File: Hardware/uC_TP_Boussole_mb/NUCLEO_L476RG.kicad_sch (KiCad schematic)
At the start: 40 parts, among them J501 Conn_01x06, J502 Conn_01x06, J503 Conn_01x06, SW501 SW_Push, SW502 SW_Push, SW503 SW_Push, SW504 SW_Push, SW505 SW_Push, U501 NUCLEO_L476RG

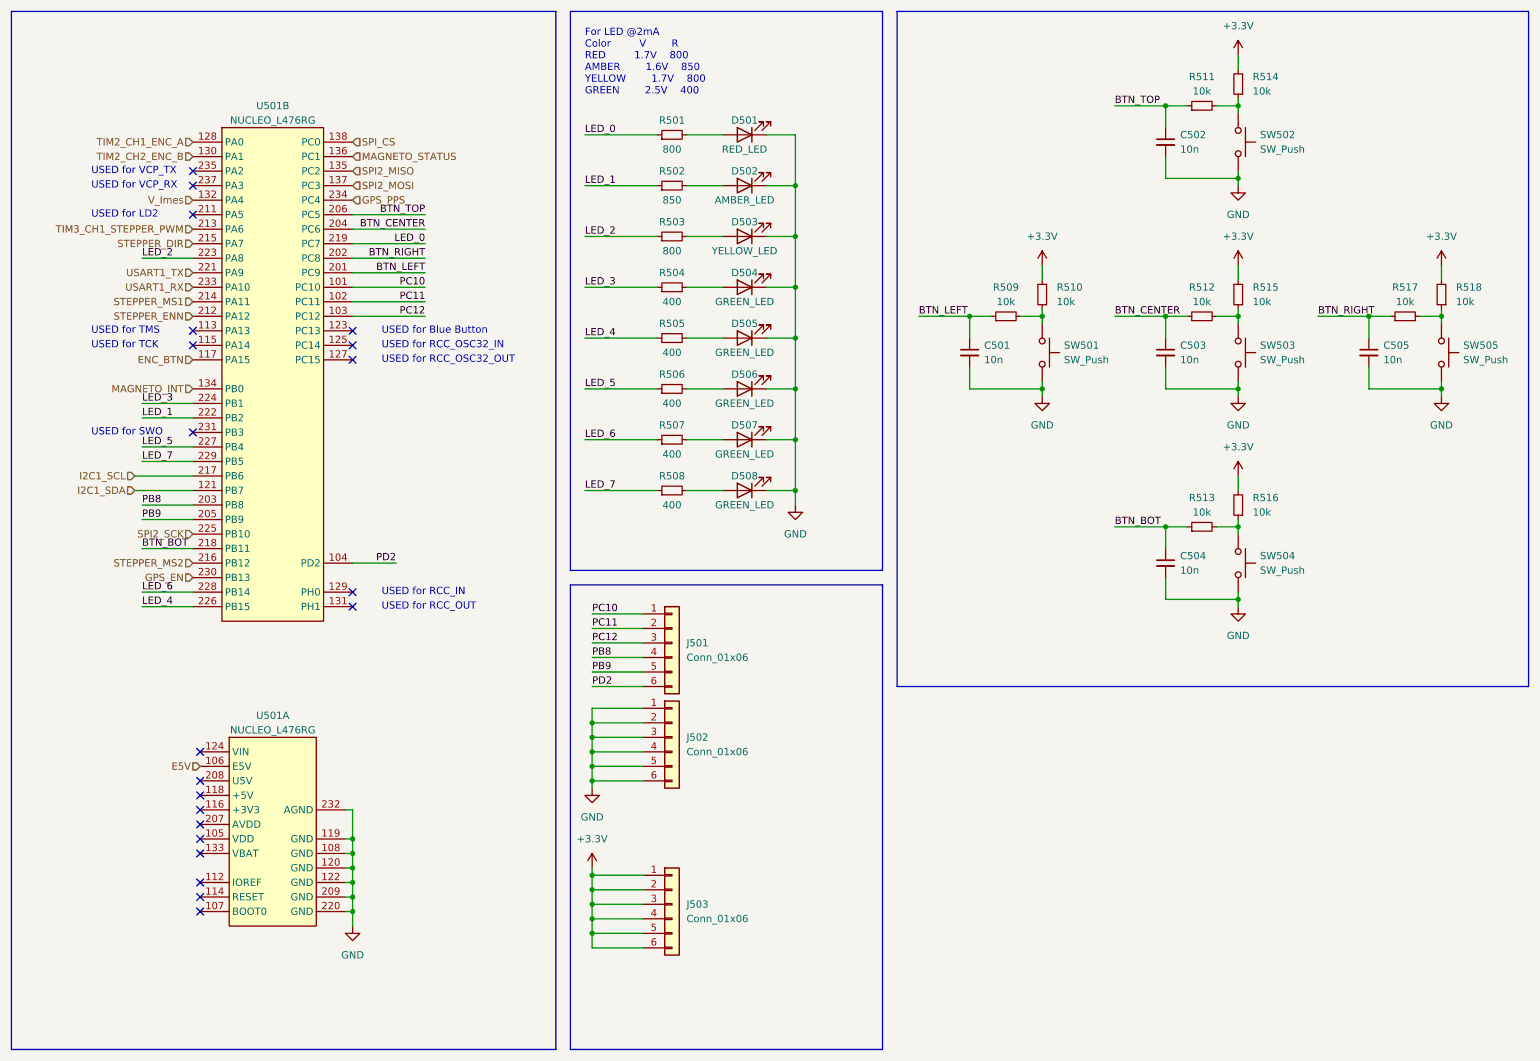
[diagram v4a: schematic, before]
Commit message: update schematic
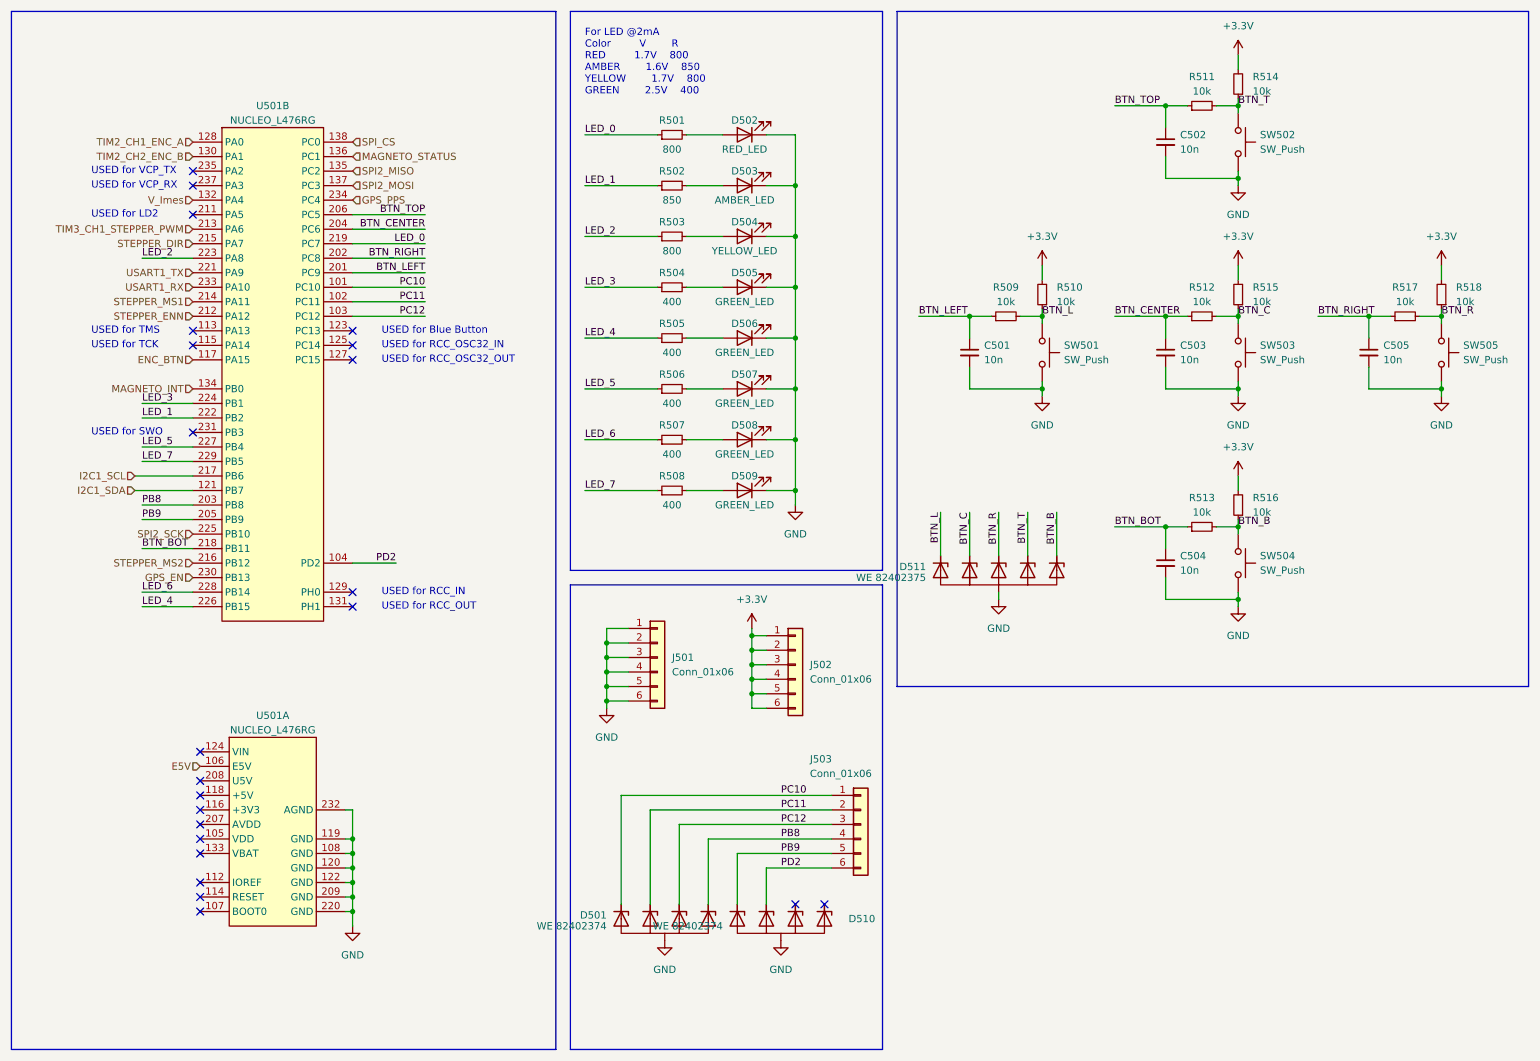
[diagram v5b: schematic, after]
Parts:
- added D501, D510: WE 82402374, libs:SC70-5L, symbol mylibs:D_TVS_Uni_x4
- added D511: WE 82402375, libs:SC70-6L, symbol mylibs:D_TVS_Uni_x5
- renumbered D501 to D502, D502 to D503, D503 to D504, D504 to D505, D505 to D506, D506 to D507, D507 to D508, D508 to D509, J502 to J501, J503 to J502, J501 to J503
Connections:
- net GND: now also D501.2 (GND), D510.2 (GND), D511.2 (GND)
- net PB8: now also D501.1 (I/O)
- net PB9: now also D510.5 (I/O)
- net PC10: now also D501.5 (I/O)
- net PC11: now also D501.4 (I/O)
- net PC12: now also D501.3 (I/O)
- net PD2: now also D510.4 (I/O)
- net BTN_R: now reaches R517.2, R518.1, SW505.1
- net BTN_R: now also D511.4 (I/O)
- net BTN_C: now reaches R512.2, R515.1, SW503.1
- net BTN_C: now also D511.5 (I/O)
- net BTN_L: now reaches R509.2, R510.1, SW501.1
- net BTN_L: now also D511.6 (I/O)
- net BTN_T: now reaches R511.2, R514.1, SW502.1
- net BTN_T: now also D511.3 (I/O)
- net BTN_B: now reaches R513.2, R516.1, SW504.1
- net BTN_B: now also D511.1 (I/O)
- no-connect marks 21 -> 23
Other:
- moved on the sheet: J501, J502, J503

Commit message: finalize pcb
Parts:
- added J504: Conn_02x10_Odd_Even, Connector_PinHeader_2.54mm:PinHeader_2x10_P2.54mm_Vertical_SMD, symbol Connector_Generic:Conn_02x10_Odd_Even
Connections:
- net BTN_B: now also D511.6 (I/O); no longer D511.1 (I/O)
- net BTN_CENTER: now also U501.206 (PC5); no longer U501.204 (PC6)
- net BTN_L: now also D511.4 (I/O); no longer D511.6 (I/O)
- net BTN_LEFT: now also U501.204 (PC6); no longer U501.201 (PC9)
- net BTN_R: now also D511.1 (I/O); no longer D511.4 (I/O)
- net BTN_RIGHT: now also U501.201 (PC9); no longer U501.202 (PC8)
- net BTN_TOP: now also U501.202 (PC8); no longer U501.206 (PC5)
- net ENC_BTN: now also J504.12 (Pin_12)
- net GND: now also J504.1 (Pin_1), J504.20 (Pin_20)
- net GPS_PPS: now also J504.19 (Pin_19)
- net I2C1_SCL: now also J504.11 (Pin_11)
- net I2C1_SDA: now also J504.13 (Pin_13)
- net PB9: now also D510.4 (I/O); no longer D510.5 (I/O)
- net PC10: now also D501.3 (I/O); no longer D501.5 (I/O)
- net PC12: now also D501.5 (I/O); no longer D501.3 (I/O)
- net PD2: now also D510.5 (I/O); no longer D510.4 (I/O)
- net SPI2_MISO: now also J504.9 (Pin_9)
- net SPI2_MOSI: now also J504.7 (Pin_7)
- net SPI2_SCK: now also J504.5 (Pin_5)
- net SPI_CS: now also J504.3 (Pin_3)
- net STEPPER_DIR: now also J504.8 (Pin_8)
- net STEPPER_ENN: now also J504.2 (Pin_2)
- net STEPPER_MS1: now also J504.4 (Pin_4)
- net STEPPER_MS2: now also J504.6 (Pin_6)
- net TIM2_CH1_ENC_A: now also J504.16 (Pin_16)
- net TIM2_CH2_ENC_B: now also J504.14 (Pin_14)
- net TIM3_CH1_STEPPER_PWM: now also J504.10 (Pin_10)
- net USART1_RX: now also J504.17 (Pin_17)
- net USART1_TX: now also J504.15 (Pin_15)
- net V_Imes: now also J504.18 (Pin_18)
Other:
- moved on the sheet: D501, D510

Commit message: create BOM, update MPN
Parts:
- SW501, SW502, SW503, SW504, SW505: MPN (none) -> 430182070816
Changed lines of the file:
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@@
 			)
 		)
+		(property "MPN" "430182070816"
+			(at 229.87 73.66 90)
+			(effects
+				(font
+					(size 1.27 1.27)
+				)
+				(hide yes)
+			)
+		)
 		(pin "1"
 		)
@@
 			)
 		)
+		(property "MPN" "430182070816"
+			(at 265.43 73.66 90)
+			(effects
+				(font
+					(size 1.27 1.27)
+				)
+				(hide yes)
+			)
+		)
 		(pin "1"
 		)
@@
 			)
 		)
+		(property "MPN" "430182070816"
+			(at 195.58 73.66 90)
+			(effects
+				(font
+					(size 1.27 1.27)
+				)
+				(hide yes)
+			)
+		)
 		(pin "1"
 		)
@@
 			)
 		)
+		(property "MPN" "430182070816"
+			(at 229.87 110.49 90)
+			(effects
+				(font
+					(size 1.27 1.27)
+				)
+				(hide yes)
+			)
+		)
 		(pin "1"
 		)
@@
 			(effects
 				(font
+					(size 1.27 1.27)
+				)
+				(hide yes)
+			)
+		)
+		(property "MPN" "430182070816"
+			(at 229.87 36.83 90)
+			(effects
+				(font

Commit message: bom
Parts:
- D502: MPN 150060RS55040 -> WE 150060RS55040
- D503: MPN 150060AS55040 -> WE 150060AS55040
- D504: MPN 150060YS55040 -> WE 150060YS55040
- D505, D506, D507, D508, D509: MPN 150060GS55040 -> WE 150060GS55040
- J501, J502, J503: MPN (none) -> SAMTEC TSW-106-05-F-T
- J504: MPN 61002021121 -> WE 61002021121
- SW501, SW502, SW503, SW504, SW505: MPN 430182070816 -> WE 430182070816
- U501: MPN (none) -> TSW-119-19-T-D
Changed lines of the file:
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@@
 			)
 		)
-		(property "MPN" "150060GS55040"
+		(property "MPN" "WE 150060GS55040"
 			(at 143.51 88.9 0)
 			(effects
@@
 			)
 		)
-		(property "MPN" "150060YS55040"
+		(property "MPN" "WE 150060YS55040"
 			(at 143.51 53.34 0)
 			(effects
@@
 			)
 		)
-		(property "MPN" "430182070816"
+		(property "MPN" "WE 430182070816"
 			(at 229.87 73.66 90)
 			(effects
@@
 			)
 		)
+		(property "MPN" "TSW-119-19-T-D "
+			(at 60.96 77.47 0)
+			(effects
+				(font
+					(size 1.27 1.27)
+				)
+				(hide yes)
+			)
+		)
 		(pin "105"
 		)
@@
 			)
 		)
-		(property "MPN" "430182070816"
+		(property "MPN" "WE 430182070816"
 			(at 265.43 73.66 90)
 			(effects
@@
 			)
 		)
-		(property "MPN" "150060GS55040"
+		(property "MPN" "WE 150060GS55040"
 			(at 143.51 80.01 0)
 			(effects
@@
 			)
 		)
-		(property "MPN" "150060GS55040"
+		(property "MPN" "WE 150060GS55040"
 			(at 143.51 71.12 0)
 			(effects
@@
 			)
 		)
-		(property "MPN" "150060GS55040"
+		(property "MPN" "WE 150060GS55040"
 			(at 143.51 62.23 0)
 			(effects
@@
 			)
 		)
-		(property "MPN" "150060AS55040"
+		(property "MPN" "WE 150060AS55040"
 			(at 143.51 44.45 0)
 			(effects
@@
 			)
 		)
-		(property "MPN" "61002021121"
+		(property "MPN" "WE 61002021121"
 			(at 222.25 149.86 0)
 			(effects
@@
 			)
 		)
+		(property "MPN" "SAMTEC TSW-106-05-F-T "
+			(at 152.4 128.27 0)
+			(effects
+				(font
+					(size 1.27 1.27)
+				)
+				(hide yes)
+			)
+		)
 		(pin "5"
 		)
@@
 			)
 		)
-		(property "MPN" "430182070816"
+		(property "MPN" "WE 430182070816"
 			(at 195.58 73.66 90)
 			(effects
@@
 			)
 		)
+		(property "MPN" "SAMTEC TSW-106-05-F-T "
+			(at 163.83 156.21 0)
+			(effects
+				(font
+					(size 1.27 1.27)
+				)
+				(hide yes)
+			)
+		)
 		(pin "5"
 		)
@@
 			)
 		)
-		(property "MPN" "430182070816"
+		(property "MPN" "WE 430182070816"
 			(at 229.87 110.49 90)
 			(effects
@@
 			)
 		)
-		(property "MPN" "150060RS55040"
+		(property "MPN" "WE 150060RS55040"
 			(at 143.51 35.56 0)
 			(effects
@@
 			)
 		)
+		(property "MPN" "SAMTEC TSW-106-05-F-T "
+			(at 128.27 127 0)
+			(effects
+				(font
+					(size 1.27 1.27)
+				)
+				(hide yes)
+			)
+		)
 		(pin "5"
 		)
@@
 			)
 		)
-		(property "MPN" "150060GS55040"
+		(property "MPN" "WE 150060GS55040"
 			(at 143.51 97.79 0)
 			(effects
@@
 			)
 		)
+		(property "MPN" "TSW-119-19-T-D "
+			(at 60.96 157.48 0)
+			(effects
+				(font
+					(size 1.27 1.27)
+				)
+				(hide yes)
+			)
+		)
 		(pin "105"
 		)
@@
 			)
 		)
-		(property "MPN" "430182070816"
+		(property "MPN" "WE 430182070816"
 			(at 229.87 36.83 90)
 			(effects
